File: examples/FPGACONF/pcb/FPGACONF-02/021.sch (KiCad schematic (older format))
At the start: 25 parts, among them CN401 JST_SM04B-SRSS-TB, CN402 JST_SM04B-SRSS-TB, CN403 JST_SM04B-SRSS-TB, CN404 ZX62D-B-5PA8(30), U401 LP5907MFX-3.3/NOPB

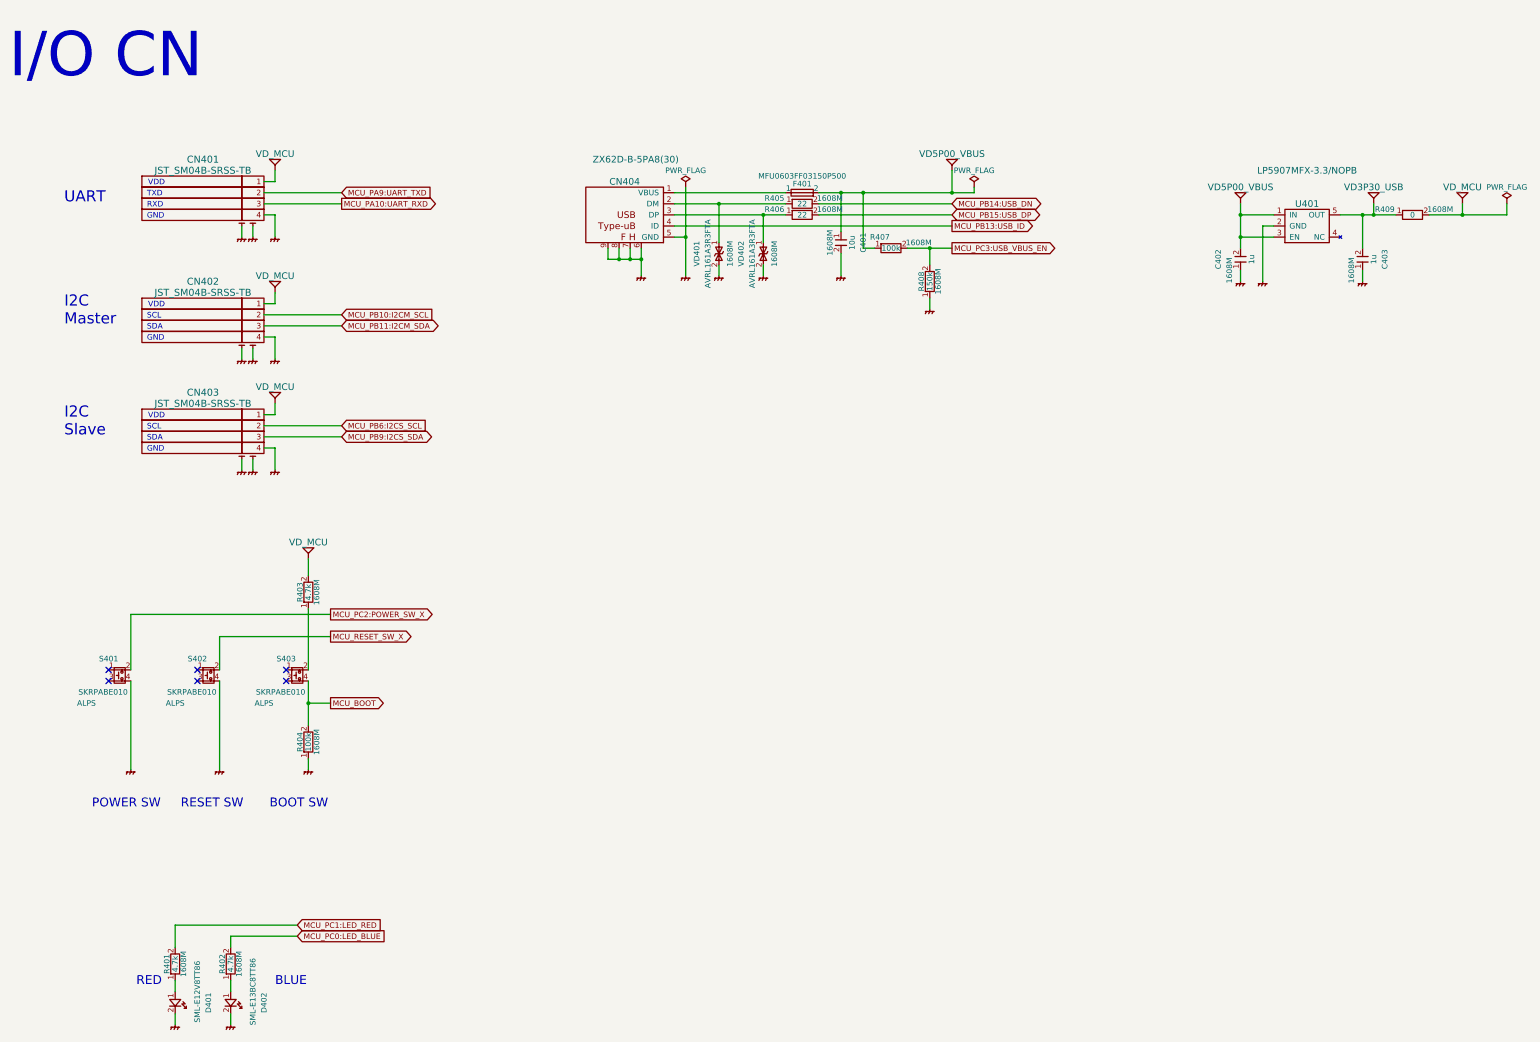
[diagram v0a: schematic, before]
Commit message: FPGACONF-02 schematics  support for SD-DDR (H743) test
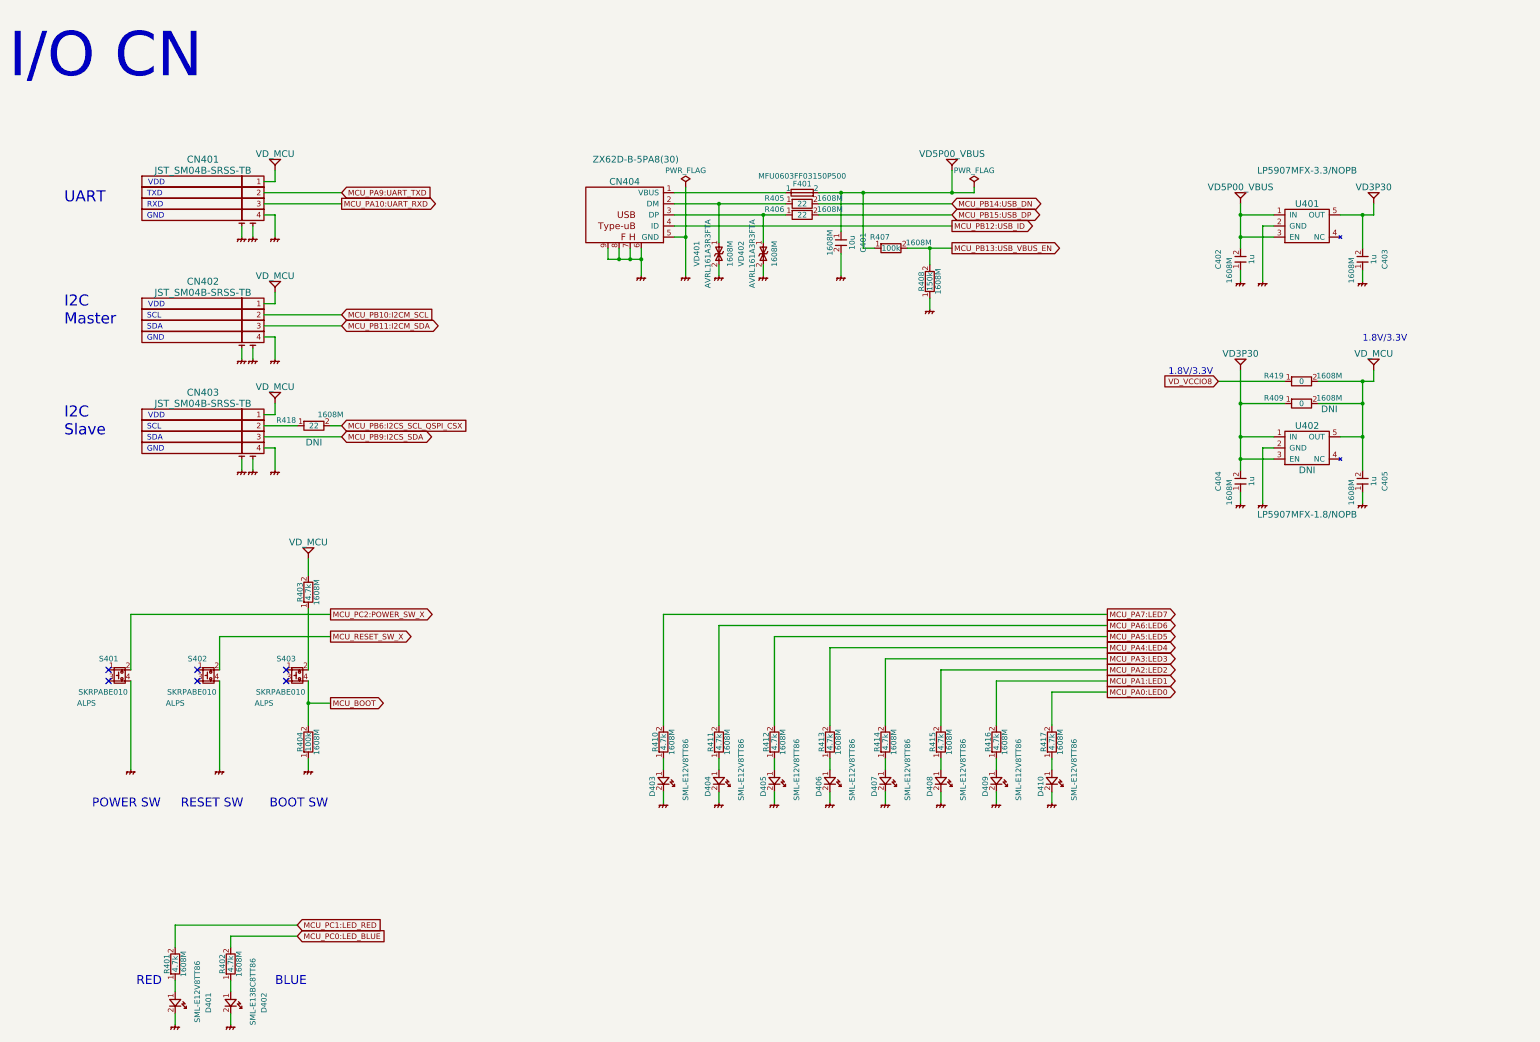
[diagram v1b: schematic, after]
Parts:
- added C404, C405: 1u, zhtlab_SMD_standard:RCL_1608m, symbol C0603
- added D403, D404, D405, D406, D407, D408, D409, D410: SML-E12V8TT86, zhtlab_SMD001-010:LED_1608M_Rohm, symbol SML-E12V8TT86
- added R410, R411, R412, R413, R414, R415, R416, R417: 4.7k, zhtlab_SMD_standard:RCL_1608m, symbol R-1608M-5%
- added R418: 22, zhtlab_SMD_standard:RCL_1608m, symbol R-1608M-5%
- added R419: 0, zhtlab_SMD_standard:RCL_1608m, symbol R-1608M-5%
- added U402: LP5907MFX-1.8/NOPB, zhtlab_SMD_standard:SOT-23-5_2.7x2.9mm_Pitch0.95mm, symbol LP5907MFX-1.8/NOPB
- R409: DNI (none) -> DNI
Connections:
- net VD_MCU: now also C405.2, R419.2, U402.5 (OUT)
- net MCU_PB13:USB_ID renamed MCU_PB12:USB_ID
- net MCU_PB6:I2CS_SCL: no longer names the net of CN403.2
- net MCU_PB6:I2CS_SCL: now also R418.1
- net MCU_PC3:USB_VBUS_EN renamed MCU_PB13:USB_VBUS_EN
- net VD3P30_USB renamed VD3P30
- net VD3P30: now also C404.2, U402.1 (IN), U402.3 (EN)
- new net: D403.1, R410.1
- new net: D404.1, R411.1
- new net: D405.1, R412.1
- new net: D406.1, R413.1
- new net: D407.1, R414.1
- new net: D408.1, R415.1
- new net: D409.1, R416.1
- new net: D410.1, R417.1
- new net MCU_PA0:LED0: R417.2
- new net MCU_PA1:LED1: R416.2
- new net MCU_PA2:LED2: R415.2
- new net MCU_PA3:LED3: R414.2
- new net MCU_PA4:LED4: R413.2
- new net MCU_PA5:LED5: R412.2
- new net MCU_PA6:LED6: R411.2
- new net MCU_PA7:LED7: R410.2
- new net MCU_PB6:I2CS_SCL_QSPI_CSX: R418.2
- new net VD_VCCIO8: R419.1
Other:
- note added: "1.8V/3.3V"
- moved on the sheet: R409
